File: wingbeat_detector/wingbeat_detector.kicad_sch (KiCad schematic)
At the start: 1 part, among them U1 OPT101P_SOCKET_RA_VERT

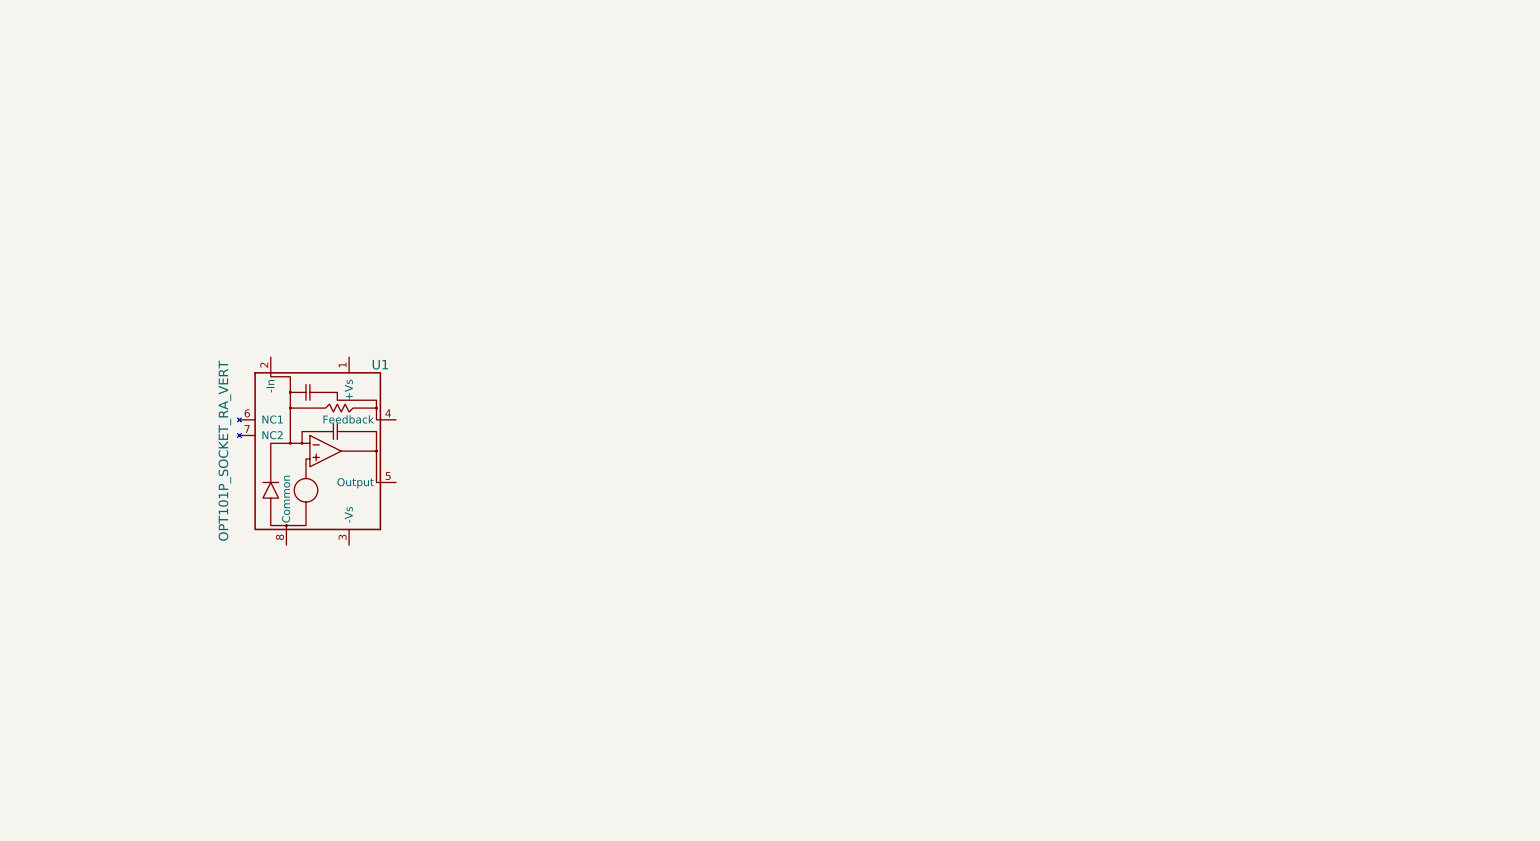
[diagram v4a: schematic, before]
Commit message: Add connectors and UAF42
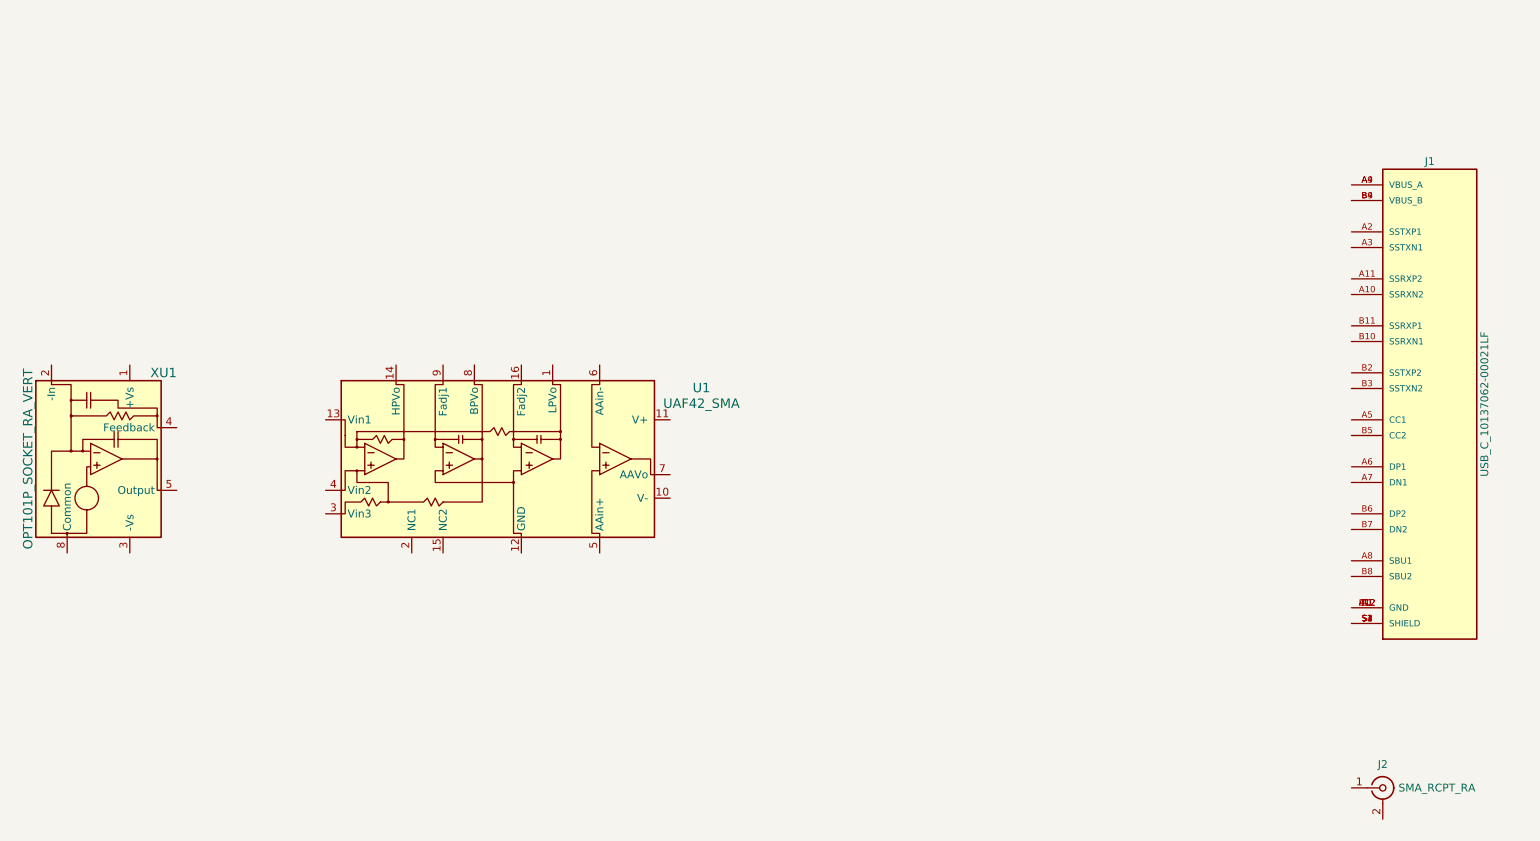
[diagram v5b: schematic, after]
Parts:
- removed U1: OPT101P_SOCKET_RA_VERT, Janelia:SOCKET_DIP_02x04_RA_VERT, symbol Janelia:OPT101P_SOCKET_RA_VERT
- added J1: USB_C_10137062-00021LF, Janelia:USB_C_Receptacle_Amphenol_10137062-00021LF, symbol Janelia:USB_C_10137062-00021LF
- added J2: SMA_RCPT_RA, Janelia:SMA_LINX_CONSMA002-G, symbol Janelia:CONN_SMA_RCPT_RA
- added U1: UAF42_SMA, Janelia:SOIC-16W_7.5x10.3mm_P1.27mm, symbol Janelia:UAF42_SMA
- added XU1: OPT101P_SOCKET_RA_VERT, Janelia:SOCKET_DIP_2x4_RA_VERT, symbol Janelia:OPT101P_SOCKET_RA_VERT
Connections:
- new net: J1.A1 (GND), J1.A12 (GND), J1.B1 (GND), J1.B12 (GND)
- new net: J1.A4 (VBUS_A), J1.A9 (VBUS_A)
- new net: J1.B4 (VBUS_B), J1.B9 (VBUS_B)
- new net: J1.S1 (SHIELD), J1.S2 (SHIELD), J1.S3 (SHIELD), J1.S4 (SHIELD)
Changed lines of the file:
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@@
   (title_block
     (title "wingbeat_detector")
-    (date "2023-02-23")
+    (date "2023-02-28")
     (rev "3.0.0")
     (company "Howard Hughes Medical Institute")
   )
-  (symbol (lib_id "Janelia:OPT101P_SOCKET_RA_VERT") (at 76.2 88.9 0) (unit 1)
+  (symbol (lib_id "Janelia:USB_C_10137062-00021LF") (at 256.54 81.28 0) (unit 1)
     (in_bom yes) (on_board yes) (dnp no)
-    (property "Reference" "U1" (at 86.36 74.93 0)
-      (effects (font (size 1.524 1.524)))
-    )
-    (property "Value" "OPT101P_SOCKET_RA_VERT" (at 60.96 88.9 90)
-      (effects (font (size 1.524 1.524)))
-    )
-    (property "Footprint" "Janelia:SOCKET_DIP_02x04_RA_VERT" (at 76.2 55.88 0)
-      (effects (font (size 1.27 1.27)) hide)
-    )
-    (property "Datasheet" "" (at 76.2 88.9 0)
-      (effects (font (size 1.27 1.27)) hide)
-    )
-    (property "Manufacturer" "Aries Electronics" (at 76.2 58.42 0)
-      (effects (font (size 1.27 1.27)) hide)
-    )
-    (property "Manufacturer Part Number" "08-810-90" (at 76.2 63.5 0)
-      (effects (font (size 1.27 1.27)) hide)
-    )
-    (property "Vendor" "Digi-Key" (at 76.2 50.8 0)
-      (effects (font (size 1.27 1.27)) hide)
-    )
-    (property "Vendor Part Number" "A117-ND" (at 76.2 60.96 0)
-      (effects (font (size 1.27 1.27)) hide)
-    )
-    (property "Description" "CONN IC DIP SOCKET 8POS GOLD" (at 76.2 53.34 0)
-      (effects (font (size 1.27 1.27)) hide)
+    (property "Reference" "J1" (at 256.54 41.91 0)
+      (effects (font (size 1.27 1.27)))
+    )
+    (property "Value" "USB_C_10137062-00021LF" (at 265.43 81.28 90)
+      (effects (font (size 1.27 1.27)))
+    )
+    (property "Footprint" "Janelia:USB_C_Receptacle_Amphenol_10137062-00021LF" (at 256.54 81.28 0)
+      (effects (font (size 1.27 1.27)) (justify left bottom) hide)
+    )
+    (property "Datasheet" "" (at 256.54 81.28 0)
+      (effects (font (size 1.27 1.27)) (justify left bottom) hide)
+    )
+    (property "Manufacturer" "Amphenol" (at 256.54 81.28 0)
+      (effects (font (size 1.27 1.27)) (justify left bottom) hide)
+    )
+    (property "Manufacturer Part Number" "10137062-00021LF" (at 256.54 81.28 0)
+      (effects (font (size 1.27 1.27)) hide)
+    )
+    (property "Vendor" "Digi-Key" (at 256.54 81.28 0)
+      (effects (font (size 1.27 1.27)) hide)
+    )
+    (property "Vendor Part Number" "609-6109-1-ND" (at 256.54 81.28 0)
+      (effects (font (size 1.27 1.27)) hide)
+    )
+    (property "Description" "CONN RCP USB3.1 TYPEC 24P SMD RA" (at 256.54 81.28 0)
+      (effects (font (size 1.27 1.27)) hide)
+    )
+    (pin "A1")
+    (pin "A10")
+    (pin "A11")
+    (pin "A12")
+    (pin "A2")
+    (pin "A3")
+    (pin "A4")
+    (pin "A5")
+    (pin "A6")
+    (pin "A7")
+    (pin "A8")
+    (pin "A9")
+    (pin "B1")
+    (pin "B10")
+    (pin "B11")
+    (pin "B12")
+    (pin "B2")
+    (pin "B3")
+    (pin "B4")
+    (pin "B5")
+    (pin "B6")
+    (pin "B7")
+    (pin "B8")
+    (pin "B9")
+    (pin "S1")
+    (pin "S2")
+    (pin "S3")
+    (pin "S4")
+    (instances
+      (project "wingbeat_detector"
+        (path "/cc457ebc-4af6-4663-b19f-8cb38f061cb4"
+          (reference "J1") (unit 1)
+        )
+      )
+    )
+  )
+  (symbol (lib_id "Janelia:CONN_SMA_RCPT_RA") (at 248.92 143.51 0) (unit 1)
+    (in_bom yes) (on_board yes) (dnp no)
+    (property "Reference" "J2" (at 248.92 139.7 0)
+      (effects (font (size 1.27 1.27)))
+    )
+    (property "Value" "SMA_RCPT_RA" (at 251.46 143.51 0)
+      (effects (font (size 1.27 1.27)) (justify left))
+    )
+    (property "Footprint" "Janelia:SMA_LINX_CONSMA002-G" (at 248.92 143.51 0)
+      (effects (font (size 1.27 1.27)) hide)
+    )
+    (property "Datasheet" "" (at 248.92 143.51 0)
+      (effects (font (size 1.27 1.27)) hide)
+    )
+    (property "Manufacturer" "Linx Technologies Inc." (at 248.92 143.51 0)
+      (effects (font (size 1.27 1.27)) hide)
+    )
+    (property "Manufacturer Part Number" "CONSMA002-G" (at 248.92 143.51 0)
+      (effects (font (size 1.27 1.27)) hide)
+    )
+    (property "Vendor" "Digi-Key" (at 248.92 143.51 0)
+      (effects (font (size 1.27 1.27)) hide)
+    )
+    (property "Vendor Part Number" "CONSMA002-G-ND" (at 248.92 143.51 0)
+      (effects (font (size 1.27 1.27)) hide)
+    )
+    (property "Description" "CONN SMA RCPT R/A 50 OHM PCB" (at 252.73 146.9782 0)
+      (effects (font (size 1.27 1.27)) (justify left) hide)
     )
     (pin "1")
+    (pin "2")
+    (instances
+      (project "wingbeat_detector"
+        (path "/cc457ebc-4af6-4663-b19f-8cb38f061cb4"
+          (reference "J2") (unit 1)
+        )
+      )
+    )
+  )
+  (symbol (lib_id "Janelia:UAF42_SMA") (at 105.41 90.17 0) (unit 1)
+    (in_bom yes) (on_board yes) (dnp no) (fields_autoplaced)
+    (property "Reference" "U1" (at 138.43 78.6383 0)
+      (effects (font (size 1.524 1.524)))
+    )
+    (property "Value" "UAF42_SMA" (at 138.43 81.1783 0)
+      (effects (font (size 1.524 1.524)))
+    )
+    (property "Footprint" "Janelia:SOIC-16W_7.5x10.3mm_P1.27mm" (at 127 78.74 0)
+      (effects (font (size 1.524 1.524)) hide)
+    )
+    (property "Datasheet" "" (at 129.54 76.2 0)
+      (effects (font (size 1.524 1.524)))
+    )
+    (property "Vendor" "Digi-Key" (at 132.08 73.66 0)
+      (effects (font (size 1.524 1.524)) hide)
+    )
+    (property "Vendor Part Number" "UAF42AU-ND" (at 134.62 71.12 0)
+      (effects (font (size 1.524 1.524)) hide)
+    )
+    (property "Description" "IC UNIV ACTIVE FILTER 16-SOIC" (at 137.16 68.58 0)
+      (effects (font (size 1.524 1.524)) hide)
+    )
+    (property "Manufacturer" "Texas Instruments" (at 105.41 90.17 0)
+      (effects (font (size 1.27 1.27)) hide)
+    )
+    (property "Manufacturer Part Number" "UAF42AU" (at 105.41 90.17 0)
+      (effects (font (size 1.27 1.27)) hide)
+    )
+    (pin "1")
+    (pin "10")
+    (pin "11")
+    (pin "12")
+    (pin "13")
+    (pin "14")
+    (pin "15")
+    (pin "16")
     (pin "2")
     (pin "3")
@@
     (pin "7")
     (pin "8")
+    (pin "9")
     (instances
       (project "wingbeat_detector"
@@
         )
       )
+    )
+  )
+  (symbol (lib_id "Janelia:OPT101P_SOCKET_RA_VERT") (at 40.64 90.17 0) (unit 1)
+    (in_bom yes) (on_board yes) (dnp no)
+    (property "Reference" "XU1" (at 53.34 76.2 0)
+      (effects (font (size 1.524 1.524)) (justify right))
+    )
+    (property "Value" "OPT101P_SOCKET_RA_VERT" (at 29.21 90.17 90)
+      (effects (font (size 1.524 1.524)))
+    )
+    (property "Footprint" "Janelia:SOCKET_DIP_2x4_RA_VERT" (at 40.64 57.15 0)
+      (effects (font (size 1.27 1.27)) hide)
+    )
+    (property "Datasheet" "" (at 40.64 90.17 0)
+      (effects (font (size 1.27 1.27)) hide)
+    )
+    (property "Manufacturer" "Aries Electronics" (at 40.64 59.69 0)
+      (effects (font (size 1.27 1.27)) hide)
+    )
+    (property "Manufacturer Part Number" "08-810-90" (at 40.64 64.77 0)
+      (effects (font (size 1.27 1.27)) hide)
+    )
+    (property "Vendor" "Digi-Key" (at 40.64 52.07 0)
+      (effects (font (size 1.27 1.27)) hide)
+    )
+    (property "Vendor Part Number" "A117-ND" (at 40.64 62.23 0)
+      (effects (font (size 1.27 1.27)) hide)
+    )
+    (property "Description" "CONN IC DIP SOCKET 8POS GOLD" (at 40.64 54.61 0)
+      (effects (font (size 1.27 1.27)) hide)
+    )
+    (pin "1")
+    (pin "2")
+    (pin "3")
+    (pin "4")
+    (pin "5")
+    (pin "8")
+    (instances
+      (project "wingbeat_detector"
+        (path "/cc457ebc-4af6-4663-b19f-8cb38f061cb4"
+          (reference "XU1") (unit 1)
+        )
+      )

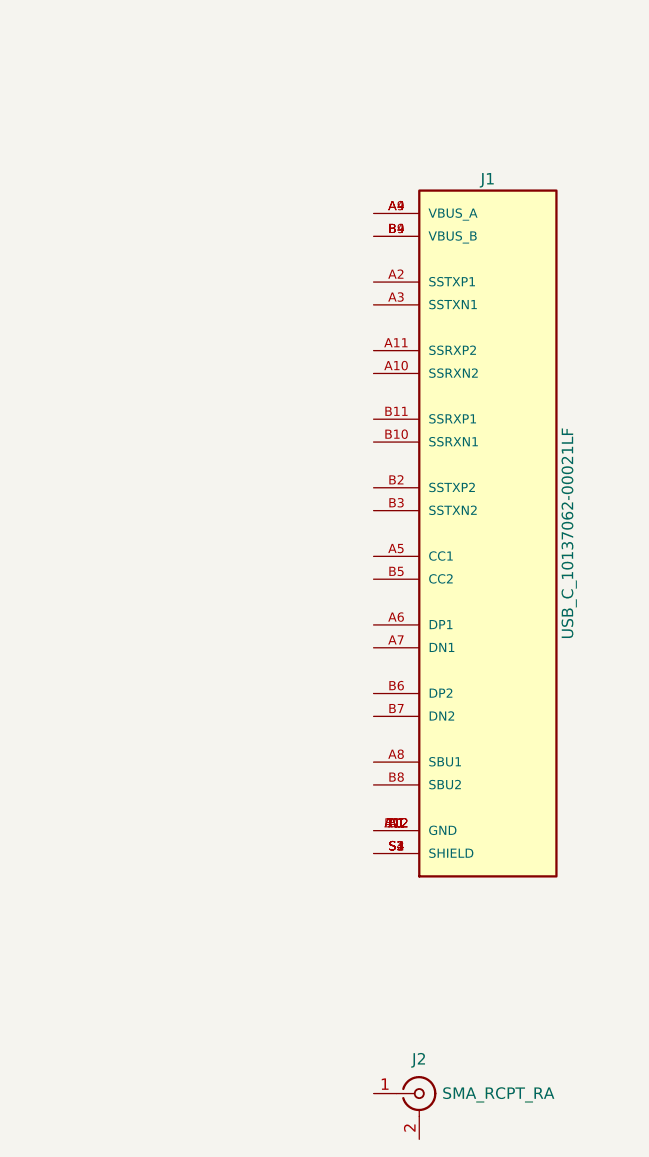
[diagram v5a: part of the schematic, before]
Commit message: Switch from SMA to UNC
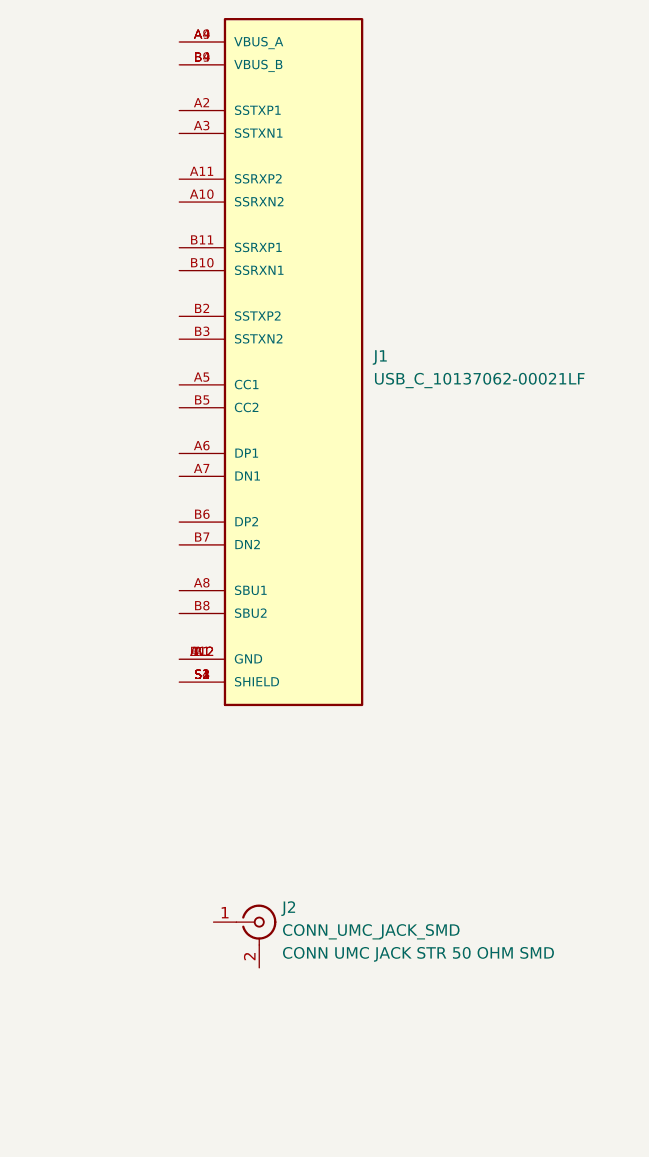
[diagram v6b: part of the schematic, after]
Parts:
- removed J2: SMA_RCPT_RA, Janelia:SMA_LINX_CONSMA002-G, symbol Janelia:CONN_SMA_RCPT_RA
- added J2: CONN_UMC_JACK_SMD, Janelia:UMC_AMPHENOL_A-1JB, symbol Janelia:CONN_UMC_JACK_SMD
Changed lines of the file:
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@@
     (company "Howard Hughes Medical Institute")
   )
-  (symbol (lib_id "Janelia:USB_C_10137062-00021LF") (at 256.54 81.28 0) (unit 1)
-    (in_bom yes) (on_board yes) (dnp no)
-    (property "Reference" "J1" (at 256.54 41.91 0)
-      (effects (font (size 1.27 1.27)))
+  (symbol (lib_id "Janelia:CONN_UMC_JACK_SMD") (at 231.14 124.46 0) (unit 1)
+    (in_bom yes) (on_board yes) (dnp no) (fields_autoplaced)
+    (property "Reference" "J2" (at 233.68 122.8482 0)
+      (effects (font (size 1.27 1.27)) (justify left))
     )
-    (property "Value" "USB_C_10137062-00021LF" (at 265.43 81.28 90)
-      (effects (font (size 1.27 1.27)))
+    (property "Value" "CONN_UMC_JACK_SMD" (at 233.68 125.3882 0)
+      (effects (font (size 1.27 1.27)) (justify left))
     )
-    (property "Footprint" "Janelia:USB_C_Receptacle_Amphenol_10137062-00021LF" (at 256.54 81.28 0)
+    (property "Footprint" "Janelia:UMC_AMPHENOL_A-1JB" (at 231.14 124.46 0)
+      (effects (font (size 1.27 1.27)) hide)
+    )
+    (property "Datasheet" "" (at 231.14 124.46 0)
+      (effects (font (size 1.27 1.27)) hide)
+    )
+    (property "Manufacturer" "Amphenol RF" (at 231.14 124.46 0)
+      (effects (font (size 1.27 1.27)) hide)
+    )
+    (property "Manufacturer Part Number" "A-1JB" (at 231.14 124.46 0)
+      (effects (font (size 1.27 1.27)) hide)
+    )
+    (property "Vendor" "Digi-Key" (at 231.14 124.46 0)
+      (effects (font (size 1.27 1.27)) hide)
+    )
+    (property "Vendor Part Number" "115-A-1JBCT-ND" (at 231.14 124.46 0)
+      (effects (font (size 1.27 1.27)) hide)
+    )
+    (property "Description" "CONN UMC JACK STR 50 OHM SMD" (at 233.68 127.9282 0)
+      (effects (font (size 1.27 1.27)) (justify left))
+    )
+    (pin "1")
+    (pin "2")
+    (instances
+      (project "wingbeat_detector"
+        (path "/cc457ebc-4af6-4663-b19f-8cb38f061cb4"
+          (reference "J2") (unit 1)
+        )
+      )
+    )
+  )
+  (symbol (lib_id "Janelia:USB_C_10137062-00021LF") (at 234.95 62.23 0) (unit 1)
+    (in_bom yes) (on_board yes) (dnp no) (fields_autoplaced)
+    (property "Reference" "J1" (at 243.84 61.595 0)
+      (effects (font (size 1.27 1.27)) (justify left))
+    )
+    (property "Value" "USB_C_10137062-00021LF" (at 243.84 64.135 0)
+      (effects (font (size 1.27 1.27)) (justify left))
+    )
+    (property "Footprint" "Janelia:USB_C_Receptacle_Amphenol_10137062-00021LF" (at 234.95 62.23 0)
       (effects (font (size 1.27 1.27)) (justify left bottom) hide)
     )
-    (property "Datasheet" "" (at 256.54 81.28 0)
+    (property "Datasheet" "" (at 234.95 62.23 0)
       (effects (font (size 1.27 1.27)) (justify left bottom) hide)
     )
-    (property "Manufacturer" "Amphenol" (at 256.54 81.28 0)
+    (property "Manufacturer" "Amphenol" (at 234.95 62.23 0)
       (effects (font (size 1.27 1.27)) (justify left bottom) hide)
     )
-    (property "Manufacturer Part Number" "10137062-00021LF" (at 256.54 81.28 0)
+    (property "Manufacturer Part Number" "10137062-00021LF" (at 234.95 62.23 0)
       (effects (font (size 1.27 1.27)) hide)
     )
-    (property "Vendor" "Digi-Key" (at 256.54 81.28 0)
+    (property "Vendor" "Digi-Key" (at 234.95 62.23 0)
       (effects (font (size 1.27 1.27)) hide)
     )
-    (property "Vendor Part Number" "609-6109-1-ND" (at 256.54 81.28 0)
+    (property "Vendor Part Number" "609-6109-1-ND" (at 234.95 62.23 0)
       (effects (font (size 1.27 1.27)) hide)
     )
-    (property "Description" "CONN RCP USB3.1 TYPEC 24P SMD RA" (at 256.54 81.28 0)
+    (property "Description" "CONN RCP USB3.1 TYPEC 24P SMD RA" (at 234.95 62.23 0)
       (effects (font (size 1.27 1.27)) hide)
     )
@@
         )
       )
-    )
-  )
-  (symbol (lib_id "Janelia:CONN_SMA_RCPT_RA") (at 248.92 143.51 0) (unit 1)
-    (in_bom yes) (on_board yes) (dnp no)
-    (property "Reference" "J2" (at 248.92 139.7 0)
-      (effects (font (size 1.27 1.27)))
-    )
-    (property "Value" "SMA_RCPT_RA" (at 251.46 143.51 0)
-      (effects (font (size 1.27 1.27)) (justify left))
-    )
-    (property "Footprint" "Janelia:SMA_LINX_CONSMA002-G" (at 248.92 143.51 0)
-      (effects (font (size 1.27 1.27)) hide)
-    )
-    (property "Datasheet" "" (at 248.92 143.51 0)
-      (effects (font (size 1.27 1.27)) hide)
-    )
-    (property "Manufacturer" "Linx Technologies Inc." (at 248.92 143.51 0)
-      (effects (font (size 1.27 1.27)) hide)
-    )
-    (property "Manufacturer Part Number" "CONSMA002-G" (at 248.92 143.51 0)
-      (effects (font (size 1.27 1.27)) hide)
-    )
-    (property "Vendor" "Digi-Key" (at 248.92 143.51 0)
-      (effects (font (size 1.27 1.27)) hide)
-    )
-    (property "Vendor Part Number" "CONSMA002-G-ND" (at 248.92 143.51 0)
-      (effects (font (size 1.27 1.27)) hide)
-    )
-    (property "Description" "CONN SMA RCPT R/A 50 OHM PCB" (at 252.73 146.9782 0)
-      (effects (font (size 1.27 1.27)) (justify left) hide)
-    )
-    (pin "1")
-    (pin "2")
-    (instances
-      (project "wingbeat_detector"
-        (path "/cc457ebc-4af6-4663-b19f-8cb38f061cb4"
-          (reference "J2") (unit 1)
-        )
-      )
